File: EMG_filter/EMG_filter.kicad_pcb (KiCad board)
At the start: 2 copper layers, 84.5 x 33 mm, 13 parts

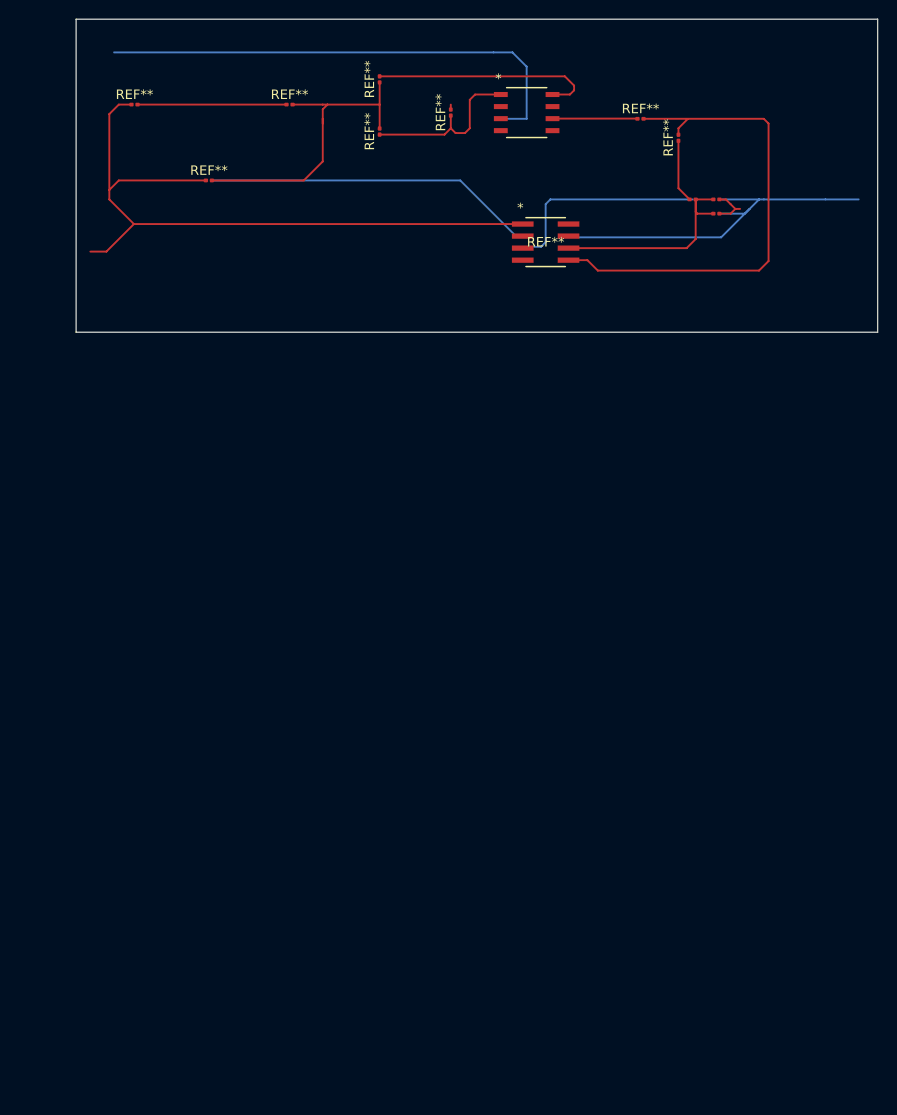
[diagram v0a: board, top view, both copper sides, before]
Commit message: First PCB design
Circuit just needs to be connected with input output and power
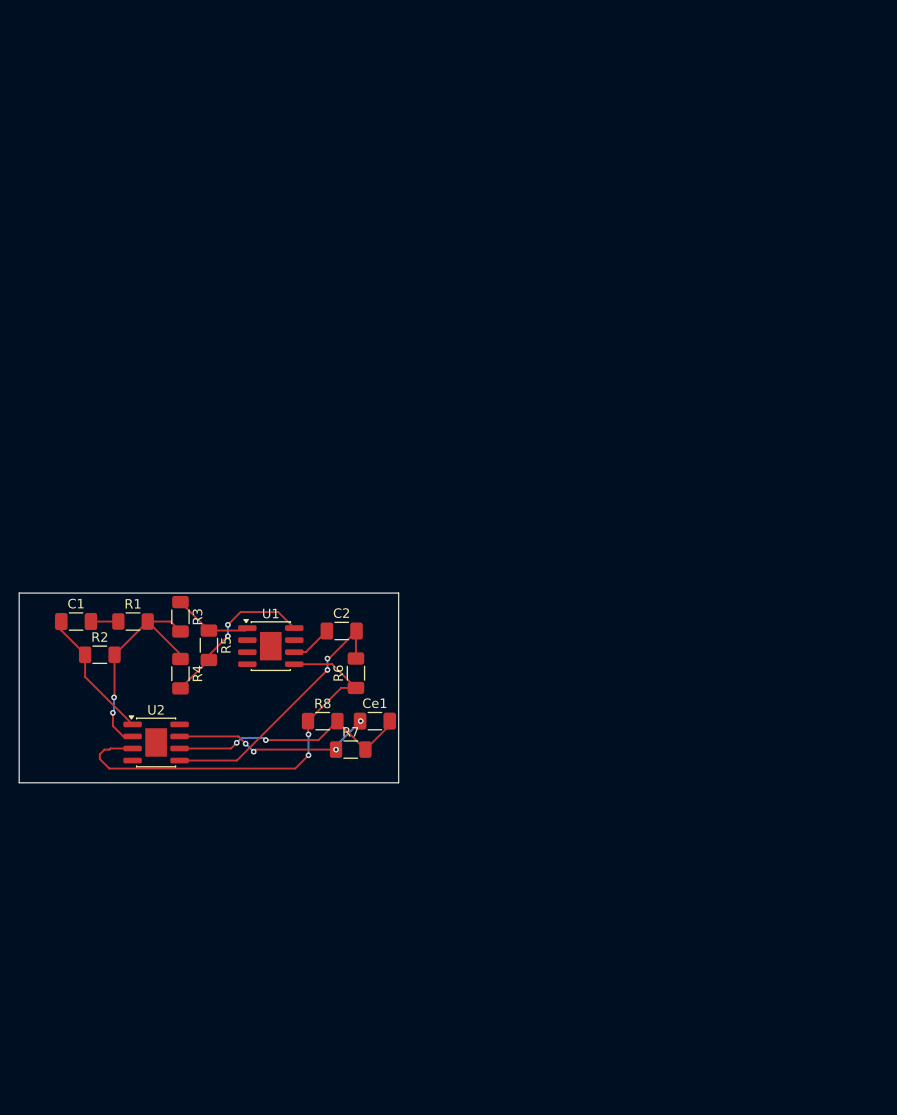
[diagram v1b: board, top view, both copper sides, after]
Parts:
- removed REF** (x8): R_0201_0603Metric, Resistor_SMD:R_0201_0603Metric
- removed REF** (x3): C_0201_0603Metric, Capacitor_SMD:C_0201_0603Metric
- removed REF**: SOIC8-N_MC_MCH, shared_footprints:SOIC8-N_MC_MCH-M
- removed REF**: SO-8_S_LIT, shared_footprints:SO-8_S_LIT
- added C1: .01uf, Capacitor_SMD:C_1206_3216Metric_Pad1.33x1.80mm_HandSolder, F.Cu at (94.5, 114.5)
- added C2: .47uf, Capacitor_SMD:C_1206_3216Metric_Pad1.33x1.80mm_HandSolder, F.Cu at (122.5, 115.5)
- added Ce1: 15nf, Capacitor_SMD:C_1206_3216Metric_Pad1.33x1.80mm_HandSolder, F.Cu at (126.0, 125.0)
- added R1: 12k, Resistor_SMD:R_1206_3216Metric_Pad1.30x1.75mm_HandSolder, F.Cu at (100.5, 114.5)
- added R2: 1M, Resistor_SMD:R_1206_3216Metric_Pad1.30x1.75mm_HandSolder, F.Cu at (97.0, 118.0)
- added R3: 30k, Resistor_SMD:R_1206_3216Metric_Pad1.30x1.75mm_HandSolder, F.Cu at (105.5, 114.0)
- added R4: 30k, Resistor_SMD:R_1206_3216Metric_Pad1.30x1.75mm_HandSolder, F.Cu at (105.5, 120.0)
- added R5: 6k, Resistor_SMD:R_1206_3216Metric_Pad1.30x1.75mm_HandSolder, F.Cu at (108.5, 117.0)
- added R6: 1M, Resistor_SMD:R_1206_3216Metric_Pad1.30x1.75mm_HandSolder, F.Cu at (124.0, 120.0)
- added R7: 10k, Resistor_SMD:R_1206_3216Metric_Pad1.30x1.75mm_HandSolder, F.Cu at (123.5, 128.0)
- added R8: 100, Resistor_SMD:R_1206_3216Metric_Pad1.30x1.75mm_HandSolder, F.Cu at (120.5, 125.0)
- added U1: AD620, Package_SO:SOIC-8-1EP_3.9x4.9mm_P1.27mm_EP2.29x3mm, F.Cu at (115.0, 117.1)
- added U2: MCP6022, Package_SO:SOIC-8-1EP_3.9x4.9mm_P1.27mm_EP2.29x3mm, F.Cu at (102.9, 127.2)
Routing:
- net (no net): track 407.2 -> 0.00 mm
- net +2V5: track 0.00 -> 44.9 mm, vias 0 -> 2
- net Net-(U2B-+): track 0.00 -> 27.9 mm, vias 0 -> 2
- net Net-(U2B--): track 0.00 -> 26.3 mm, vias 0 -> 2
- net Net-(U2A--): track 0.00 -> 24.3 mm, vias 0 -> 2
- net Net-(Ce1-Pad1): track 0.00 -> 21.5 mm, vias 0 -> 4
- net Net-(R4-Pad2): track 0.00 -> 17.0 mm, vias 0 -> 2
- net GND: track 0.00 -> 14.0 mm
- net Net-(R3-Pad1): track 0.00 -> 8.40 mm
- net Net-(C2-Pad1): track 0.00 -> 4.36 mm
- net Net-(C1-Pad2): track 0.00 -> 2.89 mm
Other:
- board size 84.5 x 33 mm -> 40 x 20 mm

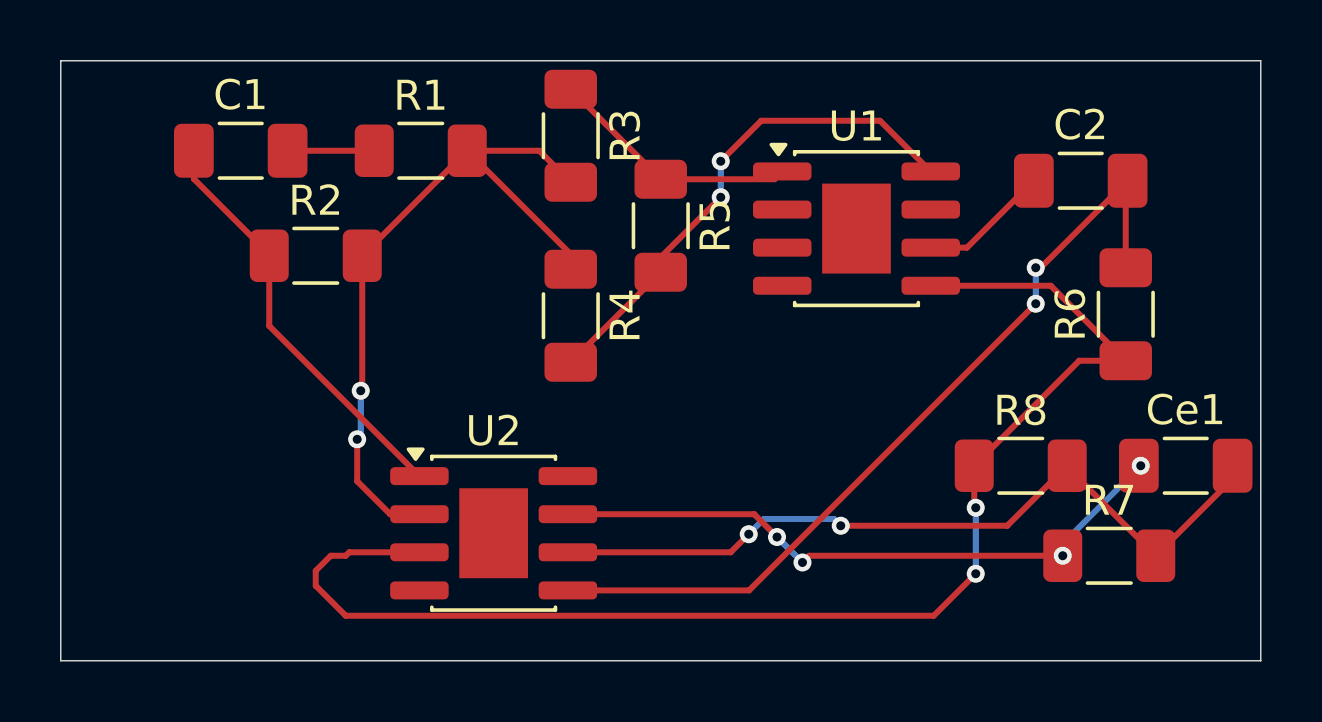
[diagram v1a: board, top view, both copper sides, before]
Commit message: Update EMG_filter.kicad_pcb
moved it so it dosent collide with border
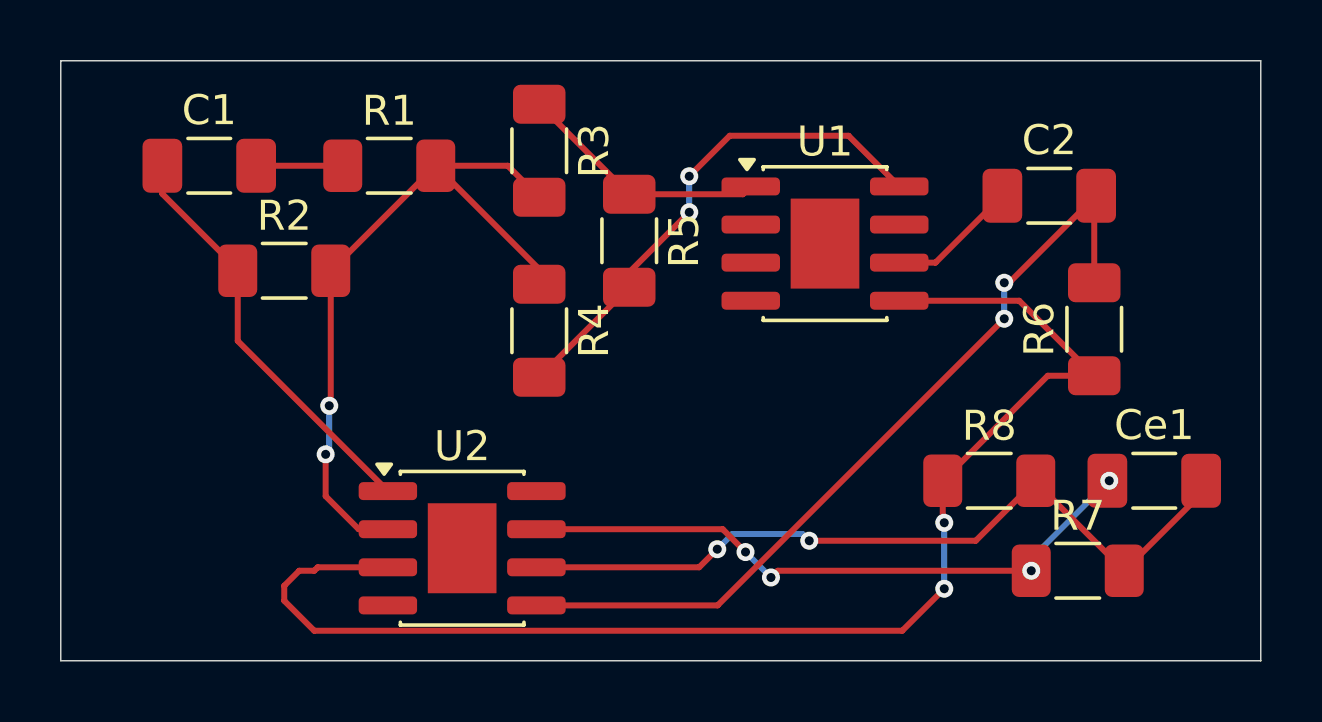
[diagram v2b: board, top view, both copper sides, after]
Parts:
- moved U1 1.16 mm to (114.0, 117.6)
- moved U2 1.16 mm to (101.9, 127.8)
- moved C1 1.16 mm to (93.5, 115.0)
- moved C2 1.16 mm to (121.5, 116.0)
- moved Ce1 1.16 mm to (125.0, 125.5)
- moved R1 1.16 mm to (99.5, 115.0)
- moved R2 1.16 mm to (96.0, 118.5)
- moved R3 1.16 mm to (104.5, 114.5)
- moved R4 1.16 mm to (104.5, 120.5)
- moved R5 1.16 mm to (107.5, 117.5)
- moved R6 1.16 mm to (123.0, 120.5)
- moved R7 1.16 mm to (122.4, 128.5)
- moved R8 1.16 mm to (119.5, 125.5)

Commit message: minimized pcb
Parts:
- C1, C2, Ce1: footprint Capacitor_SMD:C_1206_3216Metric_Pad1.33x1.80mm_HandSolder -> Capacitor_SMD:C_0201_0603Metric_Pad0.64x0.40mm_HandSolder
- R1, R2, R3, R4, R5, R6, R7, R8: footprint Resistor_SMD:R_1206_3216Metric_Pad1.30x1.75mm_HandSolder -> Resistor_SMD:R_0201_0603Metric_Pad0.64x0.40mm_HandSolder
- moved C1 37.0 mm to (102.0, 151.0)
- moved R3 37.0 mm to (106.0, 151.4)
- moved R1 36.3 mm to (104.1, 151.0)
- moved C2 36.2 mm to (117.5, 152.0)
- moved U1 35.7 mm to (112.4, 153.2)
- moved R5 34.9 mm to (107.5, 152.4)
- moved R2 34.2 mm to (103.1, 152.0)
- moved R6 33.5 mm to (118.0, 153.6)
- moved Ce1 33.2 mm to (118.1, 158.0)
- moved R4 33.1 mm to (106.0, 153.6)
- moved R8 32.7 mm to (115.6, 158.0)
- moved U2 32.4 mm to (106.9, 159.8)
- moved R7 31.5 mm to (117.0, 159.5)
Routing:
- net Net-(U2B--): track 26.3 -> 4.04 mm, vias 2 -> 0
- net +2V5: track 44.9 -> 30.2 mm
- net Net-(Ce1-Pad1): track 21.5 -> 9.54 mm, vias 4 -> 2
- net Net-(U2A--): track 24.3 -> 14.7 mm
- net Net-(U2B-+): track 27.9 -> 19.5 mm
- net GND: track 14.0 -> 8.19 mm
- net Net-(R4-Pad2): track 17.0 -> 12.0 mm
- net Net-(R3-Pad1): track 8.40 -> 4.65 mm
- net Net-(C1-Pad2): track 2.89 -> 1.25 mm
- net Net-(C2-Pad1): track 4.36 -> 3.36 mm
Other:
- board size 40 x 20 mm -> 18.5 x 14.5 mm

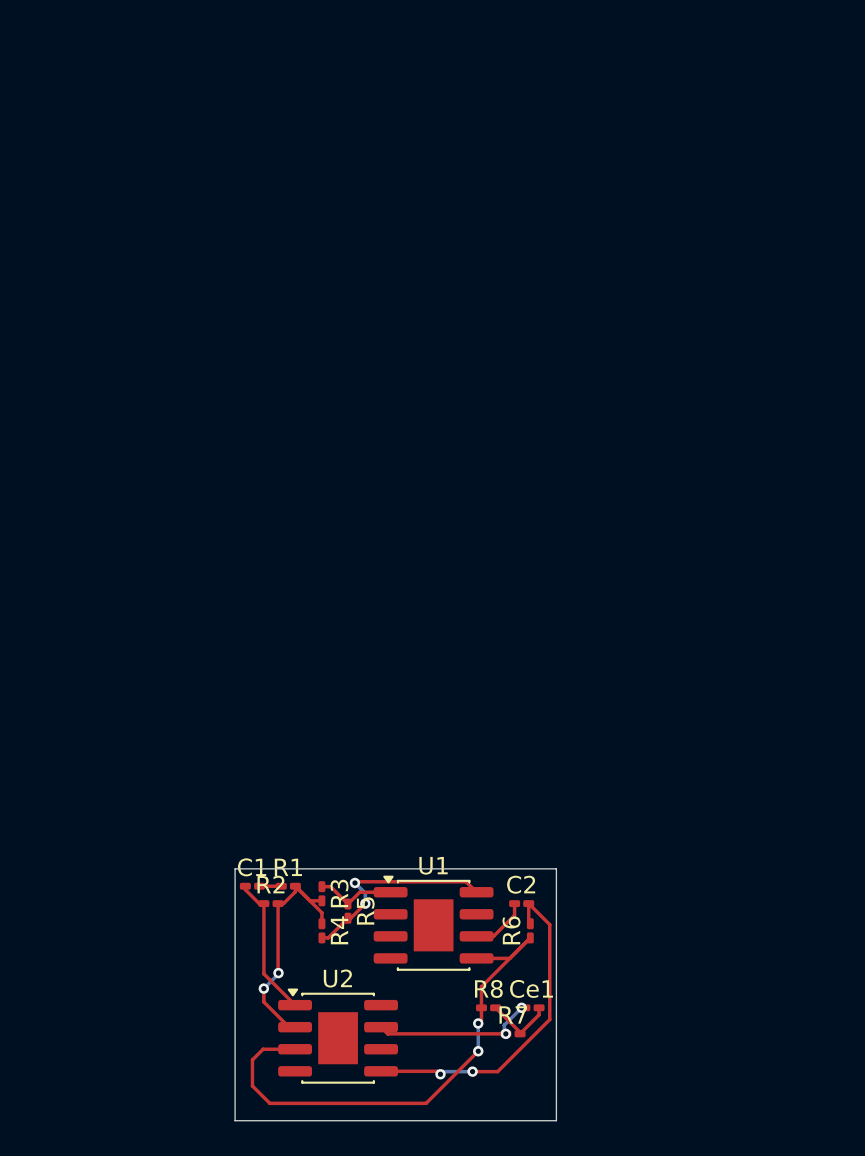
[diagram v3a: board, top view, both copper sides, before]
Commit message: Remodeled PCB to have i/o
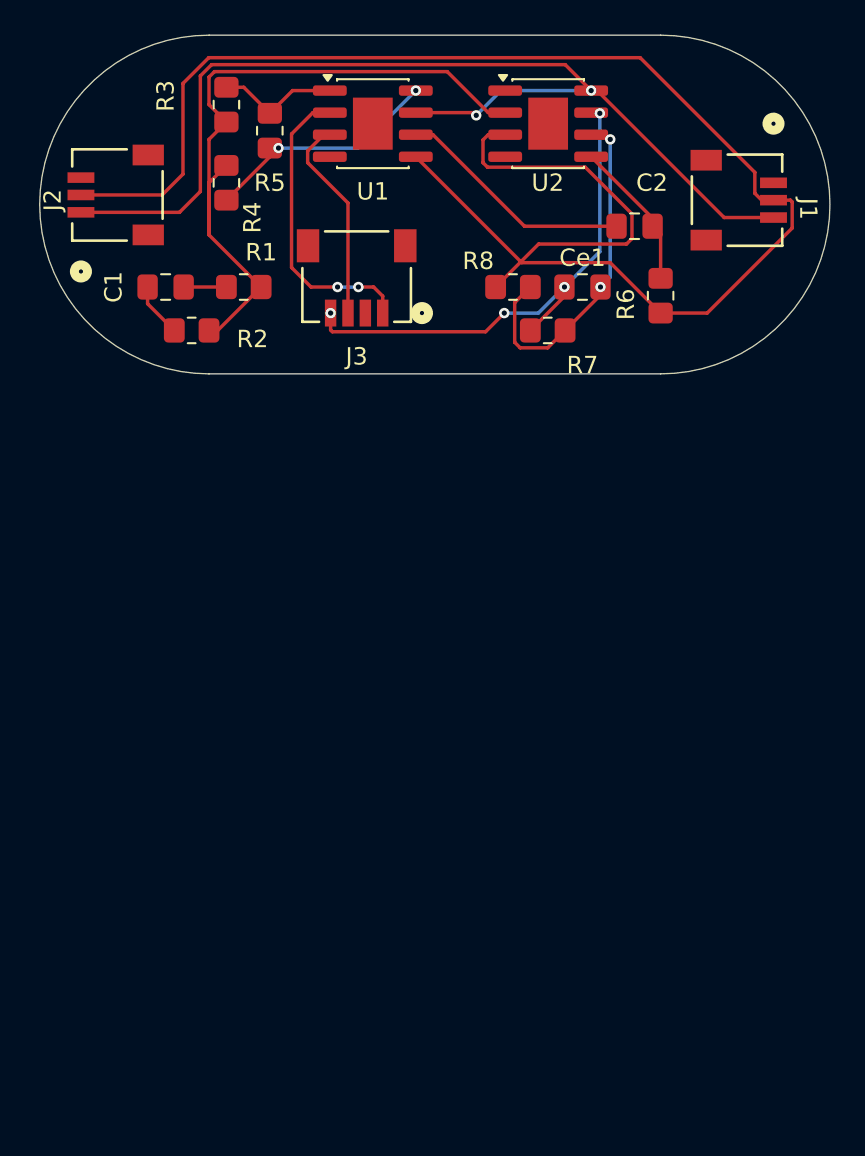
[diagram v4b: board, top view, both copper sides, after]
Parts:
- added J1: Conn_01x03_Pin, shared_footprints:CONN_SM03B-SRSS-TB_JST, F.Cu at (129.9, 111.5)
- added J2: Conn_01x03_Pin, shared_footprints:CONN_SM03B-SRSS-TB_JST, F.Cu at (94.2, 111.2)
- added J3: Conn_01x04_Pin, shared_footprints:CONN_SM04B-SRSS-TB_JST, F.Cu at (108.0, 115.9)
- C1, C2, Ce1: footprint Capacitor_SMD:C_0201_0603Metric_Pad0.64x0.40mm_HandSolder -> Capacitor_SMD:C_0805_2012Metric_Pad1.18x1.45mm_HandSolder
- R1, R2, R3, R4, R5, R6, R7, R8: footprint Resistor_SMD:R_0201_0603Metric_Pad0.64x0.40mm_HandSolder -> Resistor_SMD:R_0805_2012Metric_Pad1.20x1.40mm_HandSolder
- moved U2 54.0 mm to (119.0, 107.1)
- moved U1 46.3 mm to (108.9, 107.1)
- moved R3 45.8 mm to (100.5, 106.0)
- moved R5 45.2 mm to (103.0, 107.5)
- moved R4 43.4 mm to (100.5, 110.5)
- moved Ce1 41.6 mm to (121.0, 116.5)
- moved R8 41.5 mm to (117.0, 116.5)
- moved R7 40.5 mm to (119.0, 119.0)
- moved C2 39.5 mm to (124.0, 113.0)
- moved R6 37.3 mm to (125.5, 117.0)
- moved C1 34.9 mm to (97.0, 116.5)
- moved R1 34.6 mm to (101.5, 116.5)
- moved R2 33.3 mm to (98.5, 119.0)
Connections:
- net Net-(Ce1-Pad1) renamed Output
- U1 pad 2: -3V3 -> -In
- U1 pad 3: +3.3V -> +In
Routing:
- net +2V5: track 30.2 -> 103.3 mm, vias 2 -> 0
- net +5V: track 0.00 -> 61.7 mm, vias 0 -> 2
- net Net-(U2A--): track 14.7 -> 40.8 mm, vias 2 -> 0
- net Output: track 9.54 -> 30.2 mm, vias 2 -> 4
- net -In: track 0.00 -> 17.3 mm, vias 0 -> 2
- net Net-(U2B--): track 4.04 -> 20.3 mm, vias 0 -> 2
- net +In: track 0.00 -> 12.0 mm
- net Net-(U2B-+): track 19.5 -> 8.66 mm, vias 2 -> 0
- net Net-(C2-Pad1): track 3.36 -> 13.7 mm
- net GND: track 8.19 -> 3.14 mm
- net Net-(R3-Pad1): track 4.65 -> 7.12 mm
- net Net-(R4-Pad2): track 12.0 -> 13.8 mm
- net Net-(C1-Pad2): track 1.25 -> 2.46 mm
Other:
- board size 18.5 x 14.5 mm -> 45.5 x 19.5 mm

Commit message: new filter
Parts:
- U1, U2: footprint Package_SO:SOIC-8-1EP_3.9x4.9mm_P1.27mm_EP2.29x3mm -> Package_DIP:DIP-8_W7.62mm; moved to B.Cu
- moved R5 6.26 mm to (108.5, 104.5), turned to 180 degrees
- moved U2 5.08 mm to (123.5, 104.7), turned to 180 degrees
- moved U1 4.30 mm to (112.5, 104.7), turned to 180 degrees
- moved C2 2.50 mm to (124.0, 115.5)
- moved J3 2.46 mm to (108.8, 118.2), turned to 180 degrees
- moved R6 2.06 mm to (126.0, 119.0)
- moved Ce1 1.80 mm to (119.5, 117.5)
- moved R8 1.80 mm to (115.5, 117.5)
- moved R7 1.58 mm to (117.5, 119.5), turned to 180 degrees
- moved J1 0.92 mm to (130.7, 111.1), turned to 90 degrees
- turned J2 to -90 degrees
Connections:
- C1 pad 1: GND -> PATIENT_GND
- J1 pad 1: GND -> +5V
- J1 pad 3: +5V -> GND
- J3 pad 2: unconnected-(J3-Pin_2-Pad2) -> PATIENT_GND
- R2 pad 1: GND -> PATIENT_GND
- U2 pad 1: GND -> PATIENT_GND
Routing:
- net +2V5: track 103.3 -> 6.97 mm, vias 0 -> 4
- net PATIENT_GND: track 0.00 -> 55.5 mm, vias 0 -> 2
- net GND: track 3.14 -> 35.7 mm, vias 0 -> 1
- net +5V: track 61.7 -> 43.9 mm
- net Net-(U2B-+): track 8.66 -> 19.7 mm
- net Net-(C2-Pad1): track 13.7 -> 21.3 mm, vias 0 -> 2
- net -In: track 17.3 -> 11.0 mm
- net Net-(R3-Pad1): track 7.12 -> 13.1 mm
- net Net-(U2B--): track 20.3 -> 15.3 mm, vias 2 -> 0
- net Output: track 30.2 -> 25.4 mm, vias 4 -> 2
- net +In: track 12.0 -> 7.68 mm, vias 0 -> 2
- net Net-(U2A--): track 40.8 -> 44.5 mm
- net Net-(R4-Pad2): track 13.8 -> 11.3 mm, vias 2 -> 0
- added copper zone on B.Cu, net +2V5
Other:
- board size 45.5 x 19.5 mm -> 43 x 19.5 mm
